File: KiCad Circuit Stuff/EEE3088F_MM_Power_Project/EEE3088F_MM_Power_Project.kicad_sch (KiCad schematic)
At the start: 0 parts

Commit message: added comment
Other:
- note added: "Hi Joab"
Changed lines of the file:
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@@
 (kicad_sch (version 20230121) (generator eeschema)
   (paper "A4")
+  (text "Hi Joab\n" (at 143.002 76.454 0)
+    (effects (font (size 1.27 1.27)) (justify left bottom))
+  )
   (label "LOL" (at 139.7 95.25 0) (fields_autoplaced)
     (effects (font (size 1.27 1.27)) (justify left bottom))

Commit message: Joab Started Work on main pcb
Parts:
- added 3V3_TP1: 3V3 TP, TestPoint:TestPoint_Pad_2.5x2.5mm, symbol Connector:TestPoint
- added 5V_FB_TP1: 5V FB TP, TestPoint:TestPoint_Pad_2.5x2.5mm, symbol Connector:TestPoint
- added 5V_R1_TP1, L_TP_1, L_TP_2: ~, TestPoint:TestPoint_Pad_2.5x2.5mm, symbol Connector:TestPoint
- added 5V_R2_TP1: 5V R2 TP, TestPoint:TestPoint_Pad_2.5x2.5mm, symbol Connector:TestPoint
- added 5V_TP1: 5V TP, TestPoint:TestPoint_Pad_2.5x2.5mm, symbol Connector:TestPoint
- added 9-5V_R1_TP1: 9-5V R1 TP, TestPoint:TestPoint_Pad_2.5x2.5mm, symbol Connector:TestPoint
- added 9-5V_R2_TP1: 9-5V R2 TP, TestPoint:TestPoint_Pad_2.5x2.5mm, symbol Connector:TestPoint
- added 9-5V_VSense_TP1: 9-5V VSense TP, TestPoint:TestPoint_Pad_2.5x2.5mm, symbol Connector:TestPoint
- added 9V_TP1: 9V TP, TestPoint:TestPoint_Pad_2.5x2.5mm, symbol Connector:TestPoint
- added BAT_TP1: BAT TP, TestPoint:TestPoint_Pad_2.5x2.5mm, symbol Connector:TestPoint
- added C1, C4: 22u, Capacitor_SMD:C_1206_3216Metric_Pad1.33x1.80mm_HandSolder, symbol Device:C_Small
- added C11: 100p, Capacitor_SMD:C_0603_1608Metric_Pad1.08x0.95mm_HandSolder, symbol Device:C_Small
- added C13: TAJA106K016RNJ, JLCPCB:CAP-SMD_L3.2-W1.6-RD-C7171, symbol JLC-TAJA106K016RNJ:TAJA106K016RNJ
- added C2, C9: 10u, Capacitor_SMD:C_0603_1608Metric_Pad1.08x0.95mm_HandSolder, symbol Device:C_Small
- added C5: 10p, Capacitor_SMD:C_0603_1608Metric_Pad1.08x0.95mm_HandSolder, symbol Device:C_Small
- added C6: 220u, Capacitor_SMD:C_Elec_6.3x7.7, symbol Device:C_Polarized_Small_US
- added C7: CA45-A-10V-22UF-K, JLCPCB:CASE-A_3216, symbol JLC-CA45-A-10V-22uF-K:CA45-A-10V-22UF-K
- added C8: 4.7u, Capacitor_SMD:C_0603_1608Metric_Pad1.08x0.95mm_HandSolder, symbol Device:C_Small
- added CHRG_SelectR1_TP1, CHRG_SelectR1_TP2, CHRG_SelectR2_TP1, CHRG_SelectR2_TP2, CHRG_VinR_TP1, CHRG_VinR_TP2, Shunt_TP1, Shunt_TP2: TestPoint, TestPoint:TestPoint_Pad_2.5x2.5mm, symbol Connector:TestPoint
- added D1, D2: SS34_C8678, JLCPCB:SMA_L4.3-W2.6-LS5.2-RD, symbol JLC-SS34:SS34_C8678
- added GND_TP1: GND TP, TestPoint:TestPoint_Pad_2.5x2.5mm, symbol Connector:TestPoint
- added J1: Conn_02x16_Odd_Even, Connector_PinHeader_2.54mm:PinHeader_2x16_P2.54mm_Vertical, symbol Connector_Generic:Conn_02x16_Odd_Even
- added J2: Conn_01x02, Connector_JST:JST_PH_B2B-PH-K_1x02_P2.00mm_Vertical, symbol Connector_Generic:Conn_01x02
- added JP1: Possible Filter Cap, Jumper:SolderJumper-2_P1.3mm_Open_Pad1.0x1.5mm, symbol Jumper:Jumper_2_Open
- added JP2: Possible Filter Res2, Jumper:SolderJumper-2_P1.3mm_Open_Pad1.0x1.5mm, symbol Jumper:Jumper_2_Open
- added JP3: Possible Filter Res1, Jumper:SolderJumper-2_P1.3mm_Open_Pad1.0x1.5mm, symbol Jumper:Jumper_2_Open
- added L1: 10u, Inductor_SMD:L_Changjiang_FNR4030S, symbol Device:L_Small
- added L2: 18u, Inductor_SMD:L_Changjiang_FNR4030S, symbol Device:L_Small
- added R1: 220k, Resistor_SMD:R_0603_1608Metric_Pad0.98x0.95mm_HandSolder, symbol Device:R_Small_US
- added R10, R11: 0R, Resistor_SMD:R_0603_1608Metric_Pad0.98x0.95mm_HandSolder, symbol Device:R_Small_US
- added R12: 100m, Resistor_SMD:R_0402_1005Metric_Pad0.72x0.64mm_HandSolder, symbol Device:R_Small_US
- added R13: 2k, Resistor_SMD:R_0402_1005Metric_Pad0.72x0.64mm_HandSolder, symbol Device:R_Small_US
- added R14: 3.3k, Resistor_SMD:R_0402_1005Metric_Pad0.72x0.64mm_HandSolder, symbol Device:R_Small_US
- added R15: 2.2R, Resistor_SMD:R_0603_1608Metric_Pad0.98x0.95mm_HandSolder, symbol Device:R_Small_US
- added R16, R4: 2.2k, Resistor_SMD:R_0402_1005Metric_Pad0.72x0.64mm_HandSolder, symbol Device:R_Small_US
- added R2: 22k, Resistor_SMD:R_0603_1608Metric_Pad0.98x0.95mm_HandSolder, symbol Device:R_Small_US
- added R3: 33k, Resistor_SMD:R_0402_1005Metric_Pad0.72x0.64mm_HandSolder, symbol Device:R_Small_US
- added R5: 10k, Resistor_SMD:R_0402_1005Metric_Pad0.72x0.64mm_HandSolder, symbol Device:R_Small_US
- added R6: 1k, Resistor_SMD:R_0402_1005Metric_Pad0.72x0.64mm_HandSolder, symbol Device:R_Small_US
- added R7: 4.7R, Resistor_SMD:R_0603_1608Metric_Pad0.98x0.95mm_HandSolder, symbol Device:R_Small_US
- added U1: MT3608, Package_TO_SOT_SMD:SOT-23-6, symbol Regulator_Switching:MT3608
- added U2: AMS1117-3.3, Package_TO_SOT_SMD:SOT-223-3_TabPin2, symbol Regulator_Linear:AMS1117-3.3
- added U3: TP4056, JLCPCB:ESOP-8_L4.9-W3.9-P1.27-LS6.0-BL-EP, symbol TP4056:TP4056
- added U4: INA219AIDCNR, JLCPCB:SOT-23-8_L3.0-W1.7-P0.65-LS2.8-BR, symbol JLC-INA219AIDCNR:INA219AIDCNR
- added U6: TS5A3159DCKR, JLCPCB:SC-70-6_L2.0-W1.3-P0.65-LS2.1-BL-1, symbol JLC-TS5A3159DCKR:TS5A3159DCKR
- added U7: TPS5430DDAR, JLCPCB:ESOP-8_L4.9-W3.9-P1.27-LS6.0-TL-EP, symbol JLC-TPS5430DDAR:TPS5430DDAR
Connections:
- new net: C5.1, U7.1 (BOOT)
- new net: 9-5V_VSense_TP1.1, R4.1, R5.2, U7.4 (VSENSE)
- new net: R4.2, R6.2
- new net: D1.2 (A), L1.2, L_TP_2.1, U1.1 (SW)
- new net: U3.2 (PROG), U6.4 (COM)
- new net: 5V_FB_TP1.1, R2.2, R3.1, U1.3 (FB)
- new net: R1.2, R2.1
- new net: JP1.1 (A), JP2.1 (A), R10.2, U4.2 (IN-)
- new net: JP1.2 (B), JP3.2 (B), R11.2, U4.1 (IN+)
- new net: C9.1, CHRG_VinR_TP1.1, R15.1, R7.1
- new net: CHRG_SelectR1_TP1.1, R14.1, U6.3 (NC)
- new net: R14.2, R16.1
- new net: CHRG_SelectR2_TP1.1, R13.1, U6.1 (NO)
- new net +3V3: 3V3_TP1.1, C11.1, C7.1, J1.18 (Pin_18), U2.2 (VO), U4.4 (VS), U4.8 (A1)
- new net +5V: 5V_R1_TP1.1, 5V_TP1.1, C1.1, C13.1, D1.1 (K), J1.20 (Pin_20), R1.1, U2.3 (VI), U6.5 (V+)
- new net +9V: 9V_TP1.1, C8.2, J1.22 (Pin_22), U7.7 (VIN)
- new net Battery: BAT_TP1.1
- new net Battery_In: J1.14 (Pin_14), J2.1 (Pin_1), JP3.1 (A), R11.1, R12.2, Shunt_TP1.1
- new net Battery_Out_After_Switch: C4.1, L1.1, L_TP_1.1, U1.4 (EN), U1.5 (IN)
- new net Battery_Out_Before_Switch: C2.2, JP2.2 (B), R10.1, R12.1, Shunt_TP2.1, U3.5 (BAT)
- new net Battey_Charger_VDD: 9-5V_R1_TP1.1, C6.1, C9.2, L2.2, R5.1, U3.4 (VCC), U3.8 (CE)
- new net Fast_Charge_CTRL: J1.13 (Pin_13), U6.6 (IN)
- new net GND: 5V_R2_TP1.1, 9-5V_R2_TP1.1, C1.2, C11.2, C13.2, C2.1, C4.2, C6.2, C7.2, C8.1, CHRG_SelectR1_TP2.1, CHRG_SelectR2_TP2.1, CHRG_VinR_TP2.1, D2.2 (A), GND_TP1.1, J1.19 (Pin_19), J1.23 (Pin_23), J2.2 (Pin_2), R13.2, R15.2, R16.2, R3.2, R6.1, R7.2, U1.2 (GND), U2.1 (GND), U3.1 (TEMP), U3.3 (GND), U3.6 (STDBY#), U3.7 (CHRG#), U3.9 (EP), U4.3 (GND), U4.7 (A0), U6.2 (GND), U7.6 (GND), U7.9 (PowerPAD)
- new net I2C1_SCL: J1.16 (Pin_16), U4.5 (SCL)
- new net I2C1_SDA: J1.17 (Pin_17), U4.6 (SDA)
- new net PH_Pin: C5.2, D2.1 (K), L2.1, U7.8 (PH)
- no-connect marks 0 -> 3
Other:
- note added: "3V3 linear regulator to get 3V3 from 5V"
- note added: "5V Boost converter to obtain 5V from battery"
- note added: "Battery charging circuit"
- note added: "Connectors"
- note added: "Float enable to set default turn on"
- note added: "Global Test Points"
- note added: "INA219 Battery Monitor"
- note added: "Notes"
- note added: "PIN Layout 1: Motor2_B_Out 2: Motor2_A_Out 3: Mitir4_A_Out 4: Motor 5: Motor 6: Motor 7: CTRL_Ext_Load2 8: Motor 9: USART2_RX 10: Motor 11: EXT_Load2_Out 12: Usart2_TX 13: Fast_Charge_Ctrl 14: battery 15: rsv 16: i2C1_SCL 17: i2C1_SDA 18: 3v3 out 19: gnd 20: 5v out 21: ext_load1_out 22: HV 23: Gnd 24: motor 25: ctrl ext load1 26: motor 27: motor 28: motor 29: motor 30: motor 31: motor 32: motor"
- note added: "V0: Joab Added Circuit"
- note removed: "Hi Joab"
- company: (none) -> University Of Cape Town
- title: (none) -> EEE3088F Micro Mouse Project

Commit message: added some stuff
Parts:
- added C1 (x2): 10uF, Capacitor_SMD:C_0603_1608Metric_Pad1.08x0.95mm_HandSolder, symbol Device:C_Small
- added C11, C12, C15, C16, C7, C8: 220uF, Capacitor_SMD:C_Elec_6.3x7.7, symbol Device:C_Polarized_Small
- added C2 (x2): 2.2uF, Capacitor_SMD:C_0402_1005Metric_Pad0.74x0.62mm_HandSolder, symbol Device:C_Small
- added C3 (x2): 10nF, Capacitor_SMD:C_0402_1005Metric_Pad0.74x0.62mm_HandSolder, symbol Device:C_Small
- added C6 (x3): 100nF, Capacitor_SMD:C_0402_1005Metric_Pad0.74x0.62mm_HandSolder, symbol Device:C_Small
- added C6 (x4): 1uF, Capacitor_SMD:C_0402_1005Metric_Pad0.74x0.62mm_HandSolder, symbol Device:C_Small
- added J1: Conn_02x16_Odd_Even, symbol Connector_Generic:Conn_02x16_Odd_Even
- added R1: 75k, Resistor_SMD:R_0603_1608Metric_Pad0.98x0.95mm_HandSolder, symbol Device:R_Small
- added R1: 10k, Resistor_SMD:R_0603_1608Metric_Pad0.98x0.95mm_HandSolder, symbol Device:R_Small
- added SW1: SSSS810701, footprint:SW-SMD_SSSS810701, symbol SSSS810701:SSSS810701
- added U4: TYPE-C_16P_QTGM027, DRV8833_NEW:USB-C-SMD_TYPE-C-16P-QTGM027, symbol TYPE-C 16P QTGM027:TYPE-C_16P_QTGM027
- added U5: HUSB237-AA001-DN06R, DRV8833_NEW:TDFN-6_L2.0-W2.0-P0.65-TL-EP, symbol HUSB237_NEW:HUSB237-AA001-DN06R
- added U7 (x3): AP22814AW5-7, DRV8833_NEW:SOT-25_L3.0-W1.6-P0.95-LS2.8-BL, symbol AP22814AW5-7:AP22814AW5-7
- added U? (x2): DRV8833PWP, DRV8833_NEW:TSSOP-16_L5.0-W4.4-P0.65-LS6.4-BL-EP, symbol DRV8833_NEW:DRV8833PWP
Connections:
- net +3V3: now also J1.18 (Pin_18), U?.1 (nSleep), U?.1 (nSleep)
- net GND: now also C1.2, C1.2, C12.2, C16.2, C2.2, C2.2, C6.1, C6.1, C6.1, C6.1, C6.1, C6.1, C6.1, C8.2, J1.13 (Pin_13), J1.19 (Pin_19), R1.2, R1.2, U4.17 (EH), U4.18 (EH), U4.19 (EH), U4.20 (EH), U4.A1 (GND), U4.A12 (GND), U5.7 (GND), U7.2 (GND), U7.2 (GND), U7.2 (GND), U?.13 (GND), U?.13 (GND), U?.17 (GND), U?.17 (GND), U?.3 (AISEN), U?.3 (AISEN), U?.6 (BISEN), U?.6 (BISEN)
- new net: C15.2, C16.1
- new net: C7.2, C8.1
- new net: C2.1, U?.14 (VINT) (x2)
- new net: C3.1, U?.11 (VCP) (x2)
- new net: R1.1, U5.3 (VSET)
- new net: C11.2, C12.1
- new net 5V: C6.2, C6.2, U7.5 (IN), U7.5 (IN)
- new net AIN1 (U1): J1.28 (Pin_28)
- new net AIN1 (U2): J1.24 (Pin_24)
- new net AIN2 (U1): J1.30 (Pin_30)
- new net AIN2 (U2): J1.26 (Pin_26)
- new net AOUT1 (U1): J1.32 (Pin_32)
- new net AOUT1 (U2): J1.27 (Pin_27)
- new net AOUT2 (U1): J1.31 (Pin_31)
- new net AOUT2 (U2): J1.29 (Pin_29)
- new net BIN1 (U1): J1.4 (Pin_4)
- new net BIN1 (U2): J1.8 (Pin_8)
- new net BIN2 (U1): J1.6 (Pin_6)
- new net BIN2 (U2): J1.10 (Pin_10)
- new net BOUT1 (U1): J1.2 (Pin_2)
- new net BOUT1 (U2): J1.3 (Pin_3)
- new net BOUT2 (U1): J1.1 (Pin_1)
- new net BOUT2 (U2): J1.5 (Pin_5)
- new net CC1: U4.A5 (CC1), U5.1 (CC1)
- new net CC2: U4.B5 (CC2), U5.6 (CC2)
- new net CTRL_EXT_LOAD1: U7.4 (EN)
- new net CTRL_EXT_LOAD2: U7.4 (EN)
- new net DN1: U4.B7 (DN2)
- new net DN1/DN2: U5.5 (D-)
- new net DN2: U4.A7 (DN1)
- new net DP1: U4.B6 (DP2)
- new net DP1/DP2: U5.4 (D+)
- new net DP2: U4.A6 (DP1)
- new net EXT_LOAD1_OUT: C6.2, C7.1, U7.1 (OUT)
- new net EXT_LOAD2_OUT: C11.1, C6.2, U7.1 (OUT)
- new net MOTOR1_A_OUT: U?.2 (AOUT1)
- new net MOTOR1_B_OUT: U?.4 (AOUT2)
- new net MOTOR1_CTRL1: U?.16 (AIN1)
- new net MOTOR1_CTRL2: U?.15 (AIN2)
- new net MOTOR2_A_OUT: U?.7 (BOUT1)
- new net MOTOR2_B_OUT: U?.5 (BOUT2)
- new net MOTOR2_CTRL1: U?.9 (BIN1)
- new net MOTOR2_CTRL2: U?.10 (BIN2)
- new net MOTOR3_A_OUT: U?.2 (AOUT1)
- new net MOTOR3_B_OUT: U?.4 (AOUT2)
- new net MOTOR3_CTRL1: U?.16 (AIN1)
- new net MOTOR3_CTRL2: U?.15 (AIN2)
- new net MOTOR4_A_OUT: U?.7 (BOUT1)
- new net MOTOR4_B_OUT: U?.5 (BOUT2)
- new net MOTOR4_CTRL1: U?.9 (BIN1)
- new net MOTOR4_CTRL2: U?.10 (BIN2)
- new net MT3608 (EN): R1.1, SW1.2, U7.4 (EN)
- new net MT3608 (INPUT PIN): C15.1, C6.2, U7.1 (OUT)
- new net Power System: C6.2, U4.A9 (VBUS), U5.2 (VUSB)
- new net VBATT: C1.1, C1.1, C3.2, C3.2, C6.2, SW1.1, U7.5 (IN), U?.12 (VM), U?.12 (VM)
- new net VBUS: U4.A4 (VBUS)
- new net VM: J1.14 (Pin_14)
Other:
- note added: "1 Motor2_B_OUT 2 Motor2_A_OUT 3 Motor4_A_OUT 4 PD12/TIM4C1 MOTOR2_CTRL1 5 Motor4_B_OUT 6 PD13/TIM4C2 MOTOR2_CTRL2 7 PD2 CTRL_EXT_LOAD2 8 PD14/TIM4C3 MOTOR4_CTRL1 9 PD6/RESV USART2_RX 10 PD15/TIM4C4 MOTOR4_CTRL2 11 EXT_LOAD2_OUT 12 PD5/RESV USART2_TX 13 PB4 FAST_CHARGE_CTRL 14 Battery 15 PD7/ RESV 16 PB8 I2C1_SCL 17 PB9 I2C1_SDA 18 3V3 Out 19 GND 20 5V Out 21 EXT_LOAD1_OUT 22 HV HV 23 GND 24 PC6/T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"
- note added: "Provide 2x external load swithcing at 1A, high sided connected to 5V"
- note added: "U1 controls the two 200mA motors (Motor 1 and 2)"
- note added: "U2 controls the two 500mA auxiliary motors (Motor 3 and 4)"

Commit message: Connected All circuits, Ready for pcb design
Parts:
- removed C15, C16, C7, C8: 220uF, Capacitor_SMD:C_Elec_6.3x7.7, symbol Device:C_Polarized_Small
- removed C6 (x2): 100nF, Capacitor_SMD:C_0402_1005Metric_Pad0.74x0.62mm_HandSolder, symbol Device:C_Small
- removed C6 (x2): 1uF, Capacitor_SMD:C_0402_1005Metric_Pad0.74x0.62mm_HandSolder, symbol Device:C_Small
- removed J1: Conn_02x16_Odd_Even, symbol Connector_Generic:Conn_02x16_Odd_Even
- removed R1: 10k, Resistor_SMD:R_0603_1608Metric_Pad0.98x0.95mm_HandSolder, symbol Device:R_Small
- removed SW1: SSSS810701, footprint:SW-SMD_SSSS810701, symbol SSSS810701:SSSS810701
- removed U7 (x2): AP22814AW5-7, DRV8833_NEW:SOT-25_L3.0-W1.6-P0.95-LS2.8-BL, symbol AP22814AW5-7:AP22814AW5-7
- added C11, C12: 220uF, Capacitor_SMD:C_Elec_6.3x7.7, symbol Device:C_Polarized_Small
- added C6: 100nF, Capacitor_SMD:C_0402_1005Metric_Pad0.74x0.62mm_HandSolder, symbol Device:C_Small
- added C6: 1uF, Capacitor_SMD:C_0402_1005Metric_Pad0.74x0.62mm_HandSolder, symbol Device:C_Small
- added U11: SS-12D06-G050, JLCPCB:SW-TH_3P-P4.70_SS-12D06-G050, symbol JLC-Switch:SS-12D06-G050
- added U7: AP22814AW5-7, JLCPCB:SOT-25_L3.0-W1.6-P0.95-LS2.8-BL, symbol AP22814AW5-7:AP22814AW5-7
- U4: footprint DRV8833_NEW:USB-C-SMD_TYPE-C-16P-QTGM027 -> JLCPCB:USB-C-SMD_TYPE-C-16P-QTGM027
- U5: footprint DRV8833_NEW:TDFN-6_L2.0-W2.0-P0.65-TL-EP -> JLCPCB:TDFN-6_L2.0-W2.0-P0.65-TL-EP
- U7: footprint DRV8833_NEW:SOT-25_L3.0-W1.6-P0.95-LS2.8-BL -> JLCPCB:SOT-25_L3.0-W1.6-P0.95-LS2.8-BL
- U? (x2): footprint DRV8833_NEW:TSSOP-16_L5.0-W4.4-P0.65-LS6.4-BL-EP -> JLCPCB:TSSOP-16_L5.0-W4.4-P0.65-LS6.4-BL-EP
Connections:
- net 5V is gone; now on net +5V: C6.2, U7.5 (IN)
- net MOTOR1_A_OUT is gone; now on net AOUT1 (U1): U?.2 (AOUT1)
- net MOTOR1_B_OUT is gone; now on net AOUT2 (U1): U?.4 (AOUT2)
- net MOTOR1_CTRL1 is gone; now on net AIN1 (U1): U?.16 (AIN1)
- net MOTOR1_CTRL2 is gone; now on net AIN2 (U1): U?.15 (AIN2)
- net MOTOR2_A_OUT is gone; now on net BOUT1 (U1): U?.7 (BOUT1)
- net MOTOR2_B_OUT is gone; now on net BOUT2 (U1): U?.5 (BOUT2)
- net MOTOR2_CTRL1 is gone; now on net BIN1 (U1): U?.9 (BIN1)
- net MOTOR2_CTRL2 is gone; now on net BIN2 (U1): U?.10 (BIN2)
- net MOTOR3_A_OUT is gone; now on net AOUT1 (U2): U?.2 (AOUT1)
- net MOTOR3_B_OUT is gone; now on net AOUT2 (U2): U?.4 (AOUT2)
- net MOTOR3_CTRL1 is gone; now on net AIN2 (U2): U?.16 (AIN1)
- net MOTOR3_CTRL2 is gone; now on net AIN2 (U2): U?.15 (AIN2)
- net MOTOR4_A_OUT is gone; now on net BOUT1 (U2): U?.7 (BOUT1)
- net MOTOR4_B_OUT is gone; now on net BOUT2 (U2): U?.5 (BOUT2)
- net MOTOR4_CTRL1 is gone; now on net BIN1 (U2): U?.9 (BIN1)
- net MOTOR4_CTRL2 is gone; now on net BIN2 (U2): U?.10 (BIN2)
- net Power System is gone; now on net +9V: C6.2, U4.A9 (VBUS), U5.2 (VUSB)
- net VBATT is gone; now on net Battery_Out_After_Switch: C1.1, C1.1, C3.2, C3.2, U?.12 (VM), U?.12 (VM)
- net VBUS is gone; now on net +9V: U4.A4 (VBUS)
- net +5V: now also C6.2, U7.5 (IN)
- net AIN1 (U1): now also J1.28 (Pin_28)
- net AIN1 (U2): now also J1.24 (Pin_24)
- net AIN2 (U1): now also J1.30 (Pin_30)
- net AIN2 (U2): now also J1.26 (Pin_26)
- net AOUT1 (U1): now also J1.32 (Pin_32)
- net AOUT1 (U2): now also J1.27 (Pin_27)
- net AOUT2 (U1): now also J1.31 (Pin_31)
- net AOUT2 (U2): now also J1.29 (Pin_29)
- net BIN1 (U1): now also J1.4 (Pin_4)
- net BIN1 (U2): now also J1.8 (Pin_8)
- net BIN2 (U1): now also J1.6 (Pin_6)
- net BIN2 (U2): now also J1.10 (Pin_10)
- net BOUT1 (U1): now also J1.2 (Pin_2)
- net BOUT1 (U2): now also J1.3 (Pin_3)
- net BOUT2 (U1): now also J1.1 (Pin_1)
- net BOUT2 (U2): now also J1.5 (Pin_5)
- net Battery_Out_After_Switch: now also U11.1
- net Battery_Out_Before_Switch: now also U11.2
- net CTRL_EXT_LOAD1: now also J1.25 (Pin_25), U7.4 (EN)
- net CTRL_EXT_LOAD2: now also J1.7 (Pin_7)
- net EXT_LOAD1_OUT: now also J1.21 (Pin_21), C11.1, C6.2, U7.1 (OUT)
- net EXT_LOAD2_OUT: now also J1.11 (Pin_11)
- net GND: now also C12.2, C6.1, C6.1, U11.3, U7.2 (GND)
- new net: C11.2, C12.1
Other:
- moved on the sheet: C1, C11, C12, C2, C3, C6, R1, U4, U5, U7, U?

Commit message: Done Significant circuit work
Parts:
- R12: footprint Resistor_SMD:R_0402_1005Metric_Pad0.72x0.64mm_HandSolder -> Resistor_SMD:R_1206_3216Metric_Pad1.30x1.75mm_HandSolder
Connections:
- net DN1/DN2 is gone; now on net DN1: U5.5 (D-)
- net DN2 is gone; now on net DN1: U4.A7 (DN1)
- net DP1/DP2 is gone; now on net DP1: U5.4 (D+)
- net DP2 is gone; now on net DP1: U4.A6 (DP1)
- net +5V: no longer U6.5 (V+)
- net AIN1 (U2): now also U?.16 (AIN1)
- net AIN2 (U2): no longer U?.16 (AIN1)
- net Battey_Charger_VDD: now also U6.5 (V+)
- net Battery_In renamed Battery_In_After_Switch
- net Battery_In_After_Switch: now also U11.1; no longer J1.14 (Pin_14), J2.1 (Pin_1)
- net Battery_Out_After_Switch renamed Battery_Out
- net Battery_Out: now also C2.2, J1.14 (Pin_14), JP2.2 (B), R10.1, R12.1, Shunt_TP2.1, U3.5 (BAT); no longer U11.1
- removed net Battery_Out_Before_Switch: C2.2, JP2.2 (B), R10.1, R12.1, Shunt_TP2.1, U11.2, U3.5 (BAT)
- new net Battery_In_Before_Switch: J2.1 (Pin_1), U11.2

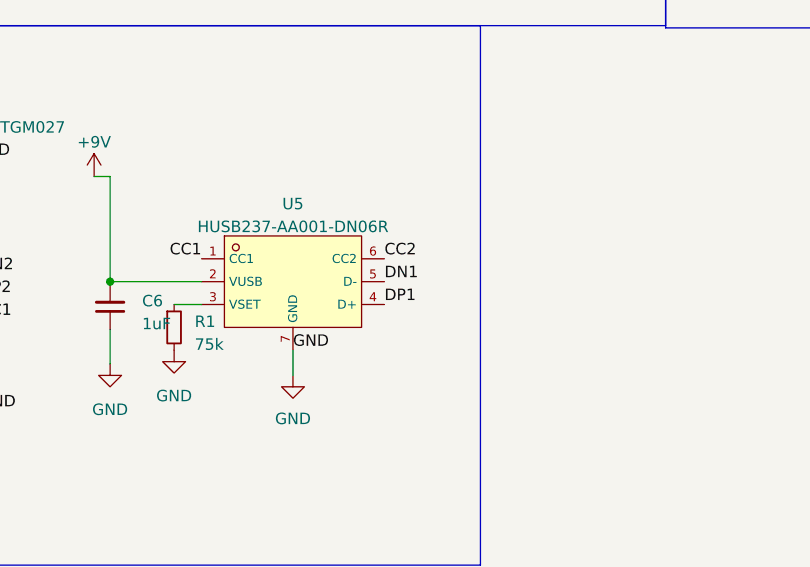
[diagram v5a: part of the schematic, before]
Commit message: Removed D+ and D- to float on the USPD
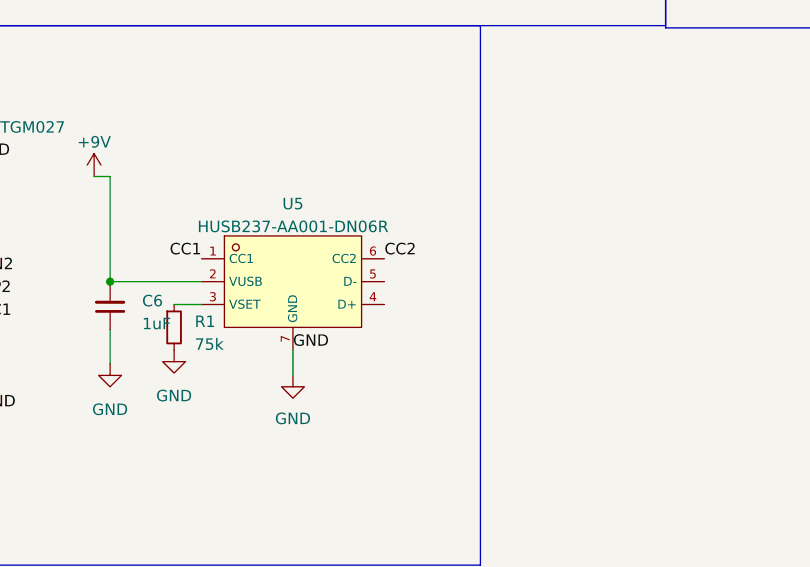
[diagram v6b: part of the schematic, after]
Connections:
- net DN1: no longer U5.5 (D-)
- net DP1: no longer U5.4 (D+)
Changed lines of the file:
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@@
     (effects (font (size 0.5 0.5)) (justify left bottom))
-  )
-  (label "DP1" (at 377.063 138.684 0) (fields_autoplaced)
-    (effects (font (size 1.27 1.27)) (justify left bottom))
   )
   (label "Battey_Charger_VDD" (at 252.73 81.915 0) (fields_autoplaced)
@@
     (effects (font (size 1.27 1.27)) (justify left bottom))
   )
-  (label "DN1" (at 377.063 136.144 0) (fields_autoplaced)
-    (effects (font (size 1.27 1.27)) (justify left bottom))
-  )
